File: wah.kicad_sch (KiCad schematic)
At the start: 32 parts, among them J3 Barrel_Jack_Switch, J4 In, J5 Out, SW2 SW_Push_3PDT, U1 L78L05_TO92, U2 TL072

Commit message: improve pcb
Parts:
- C1, C10, C11, C12, C3, C4, C5, C6, C7, C8, C9: footprint Capacitor_THT:C_Rect_L4.6mm_W2.0mm_P2.50mm_MKS02_FKP02 -> Capacitor_THT:C_Rect_L7.0mm_W2.5mm_P5.00mm
- C2: footprint Capacitor_THT:CP_Radial_D5.0mm_P2.50mm -> Capacitor_THT:C_Rect_L7.0mm_W2.5mm_P5.00mm
- R1, R2, R3, R4, R5, R6, R7, R8, R9: footprint Resistor_THT:R_Axial_DIN0207_L6.3mm_D2.5mm_P10.16mm_Horizontal -> Resistor_THT:R_Axial_DIN0207_L6.3mm_D2.5mm_P7.62mm_Horizontal
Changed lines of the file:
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@@
 		(title "Wah")
 		(date "2025-10-29")
-		(rev "0.1")
+		(rev "0.2")
 		(company "KnightHill Engineering")
 	)
@@
 			)
 		)
-		(property "Footprint" "Resistor_THT:R_Axial_DIN0207_L6.3mm_D2.5mm_P10.16mm_Horizontal"
+		(property "Footprint" "Resistor_THT:R_Axial_DIN0207_L6.3mm_D2.5mm_P7.62mm_Horizontal"
 			(at 297.18 152.908 90)
 			(effects
@@
 			)
 		)
-		(property "Footprint" "Resistor_THT:R_Axial_DIN0207_L6.3mm_D2.5mm_P10.16mm_Horizontal"
+		(property "Footprint" "Resistor_THT:R_Axial_DIN0207_L6.3mm_D2.5mm_P7.62mm_Horizontal"
 			(at 234.95 66.548 90)
 			(effects
@@
 			)
 		)
-		(property "Footprint" "Capacitor_THT:C_Rect_L4.6mm_W2.0mm_P2.50mm_MKS02_FKP02"
+		(property "Footprint" "Capacitor_THT:C_Rect_L7.0mm_W2.5mm_P5.00mm"
 			(at 168.6052 237.49 0)
 			(effects
@@
 			)
 		)
-		(property "Footprint" "Resistor_THT:R_Axial_DIN0207_L6.3mm_D2.5mm_P10.16mm_Horizontal"
+		(property "Footprint" "Resistor_THT:R_Axial_DIN0207_L6.3mm_D2.5mm_P7.62mm_Horizontal"
 			(at 78.74 65.278 90)
 			(effects
@@
 			)
 		)
-		(property "Footprint" "Resistor_THT:R_Axial_DIN0207_L6.3mm_D2.5mm_P10.16mm_Horizontal"
+		(property "Footprint" "Resistor_THT:R_Axial_DIN0207_L6.3mm_D2.5mm_P7.62mm_Horizontal"
 			(at 137.16 67.818 90)
 			(effects
@@
 			)
 		)
-		(property "Footprint" "Capacitor_THT:C_Rect_L4.6mm_W2.0mm_P2.50mm_MKS02_FKP02"
+		(property "Footprint" "Capacitor_THT:C_Rect_L7.0mm_W2.5mm_P5.00mm"
 			(at 155.9052 237.49 0)
 			(effects
@@
 			)
 		)
-		(property "Footprint" "Capacitor_THT:C_Rect_L4.6mm_W2.0mm_P2.50mm_MKS02_FKP02"
+		(property "Footprint" "Capacitor_THT:C_Rect_L7.0mm_W2.5mm_P5.00mm"
 			(at 195.2752 237.49 0)
 			(effects
@@
 			)
 		)
-		(property "Footprint" "Capacitor_THT:C_Rect_L4.6mm_W2.0mm_P2.50mm_MKS02_FKP02"
+		(property "Footprint" "Capacitor_THT:C_Rect_L7.0mm_W2.5mm_P5.00mm"
 			(at 249.8852 74.93 0)
 			(effects
@@
 			)
 		)
-		(property "Footprint" "Capacitor_THT:C_Rect_L4.6mm_W2.0mm_P2.50mm_MKS02_FKP02"
+		(property "Footprint" "Capacitor_THT:C_Rect_L7.0mm_W2.5mm_P5.00mm"
 			(at 88.5952 74.93 0)
 			(effects
@@
 			)
 		)
-		(property "Footprint" "Capacitor_THT:C_Rect_L4.6mm_W2.0mm_P2.50mm_MKS02_FKP02"
+		(property "Footprint" "Capacitor_THT:C_Rect_L7.0mm_W2.5mm_P5.00mm"
 			(at 152.4 65.0748 0)
 			(effects
@@
 			)
 		)
-		(property "Footprint" "Capacitor_THT:C_Rect_L4.6mm_W2.0mm_P2.50mm_MKS02_FKP02"
+		(property "Footprint" "Capacitor_THT:C_Rect_L7.0mm_W2.5mm_P5.00mm"
 			(at 247.3452 237.49 0)
 			(effects
@@
 			)
 		)
-		(property "Footprint" "Capacitor_THT:C_Rect_L4.6mm_W2.0mm_P2.50mm_MKS02_FKP02"
+		(property "Footprint" "Capacitor_THT:C_Rect_L7.0mm_W2.5mm_P5.00mm"
 			(at 101.6 62.5348 0)
 			(effects
@@
 			)
 		)
-		(property "Footprint" "Capacitor_THT:CP_Radial_D5.0mm_P2.50mm"
+		(property "Footprint" "Capacitor_THT:C_Rect_L7.0mm_W2.5mm_P5.00mm"
 			(at 143.2052 237.49 0)
 			(effects
@@
 			)
 		)
-		(property "Footprint" "Resistor_THT:R_Axial_DIN0207_L6.3mm_D2.5mm_P10.16mm_Horizontal"
+		(property "Footprint" "Resistor_THT:R_Axial_DIN0207_L6.3mm_D2.5mm_P7.62mm_Horizontal"
 			(at 106.172 52.07 90)
 			(effects
@@
 			)
 		)
-		(property "Footprint" "Resistor_THT:R_Axial_DIN0207_L6.3mm_D2.5mm_P10.16mm_Horizontal"
+		(property "Footprint" "Resistor_THT:R_Axial_DIN0207_L6.3mm_D2.5mm_P7.62mm_Horizontal"
 			(at 243.332 57.15 90)
 			(effects
@@
 			)
 		)
-		(property "Footprint" "Capacitor_THT:C_Rect_L4.6mm_W2.0mm_P2.50mm_MKS02_FKP02"
+		(property "Footprint" "Capacitor_THT:C_Rect_L7.0mm_W2.5mm_P5.00mm"
 			(at 216.8652 74.93 0)
 			(effects
@@
 			)
 		)
-		(property "Footprint" "Resistor_THT:R_Axial_DIN0207_L6.3mm_D2.5mm_P10.16mm_Horizontal"
+		(property "Footprint" "Resistor_THT:R_Axial_DIN0207_L6.3mm_D2.5mm_P7.62mm_Horizontal"
 			(at 223.52 229.108 90)
 			(effects
@@
 			)
 		)
-		(property "Footprint" "Capacitor_THT:C_Rect_L4.6mm_W2.0mm_P2.50mm_MKS02_FKP02"
+		(property "Footprint" "Capacitor_THT:C_Rect_L7.0mm_W2.5mm_P5.00mm"
 			(at 215.5952 237.49 0)
 			(effects
@@
 			)
 		)
-		(property "Footprint" "Resistor_THT:R_Axial_DIN0207_L6.3mm_D2.5mm_P10.16mm_Horizontal"
+		(property "Footprint" "Resistor_THT:R_Axial_DIN0207_L6.3mm_D2.5mm_P7.62mm_Horizontal"
 			(at 155.702 72.39 90)
 			(effects
@@
 			)
 		)
-		(property "Footprint" "Resistor_THT:R_Axial_DIN0207_L6.3mm_D2.5mm_P10.16mm_Horizontal"
+		(property "Footprint" "Resistor_THT:R_Axial_DIN0207_L6.3mm_D2.5mm_P7.62mm_Horizontal"
 			(at 234.188 233.68 90)
 			(effects
@@
 			)
 		)
-		(property "Footprint" "Capacitor_THT:C_Rect_L4.6mm_W2.0mm_P2.50mm_MKS02_FKP02"
+		(property "Footprint" "Capacitor_THT:C_Rect_L7.0mm_W2.5mm_P5.00mm"
 			(at 228.6 63.8048 0)
 			(effects

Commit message: improve pcb
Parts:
- added GND1, GND2: ~, TestPoint:TestPoint_THTPad_1.5x1.5mm_Drill0.7mm, symbol Connector:TestPoint
- added TP_IN1, TP_OUT1: TestPoint, TestPoint:TestPoint_THTPad_1.5x1.5mm_Drill0.7mm, symbol Connector:TestPoint
- renumbered C10 to C1, C9 to C10, C7 to C11, C8 to C12, C11 to C2, C2 to C3, C3 to C4, C4 to C5, C12 to C6, C1 to C7, C5 to C8, C6 to C9, J3 to J1, J4 to J2, J5 to J3, R6 to R1, R7 to R2, R8 to R3, R9 to R4, R4 to R5, R5 to R6, R2 to R7, R3 to R8, R1 to R9, SW2 to SW1, U2 to U1, U1 to U2
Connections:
- net FX_IN: now also TP_IN1.1
- net FX_OUT: now also TP_OUT1.1
- net GND: now also GND1.1, GND2.1
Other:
- moved on the sheet: C1, C11, C12, C2, C6, C9, R1, R2, R3, R4, R7, R8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

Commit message: fix errors
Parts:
- removed C10: 100u, Capacitor_THT:C_Rect_L7.0mm_W2.5mm_P5.00mm, symbol Device:C
- added C13: 100u, Capacitor_THT:CP_Radial_D6.3mm_P2.50mm, symbol Device:C_Polarized
- added TP_5V1, TP_VREF1: TestPoint, TestPoint:TestPoint_THTPad_1.5x1.5mm_Drill0.7mm, symbol Connector:TestPoint
- C3: footprint Capacitor_THT:C_Rect_L7.0mm_W2.5mm_P5.00mm -> Capacitor_THT:CP_Radial_D6.3mm_P2.50mm
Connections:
- net AUDIO_IN: now also C6.2, R4.1; no longer U1.1, U1.2 (-)
- net AUDIO_OUT: now also C11.1, C9.1; no longer R1.1
- net FX_IN: now also R1.1; no longer C11.1, C9.1
- net FX_OUT: now also U1.1, U1.2 (-); no longer C6.2, R4.1
- net GND: now also C13.2
- net VREF: now also C13.1, TP_VREF1.1
- net at C7.1, C8.1, R5.1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: now also TP_5V1.1
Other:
- moved on the sheet: TP_IN1, TP_OUT1

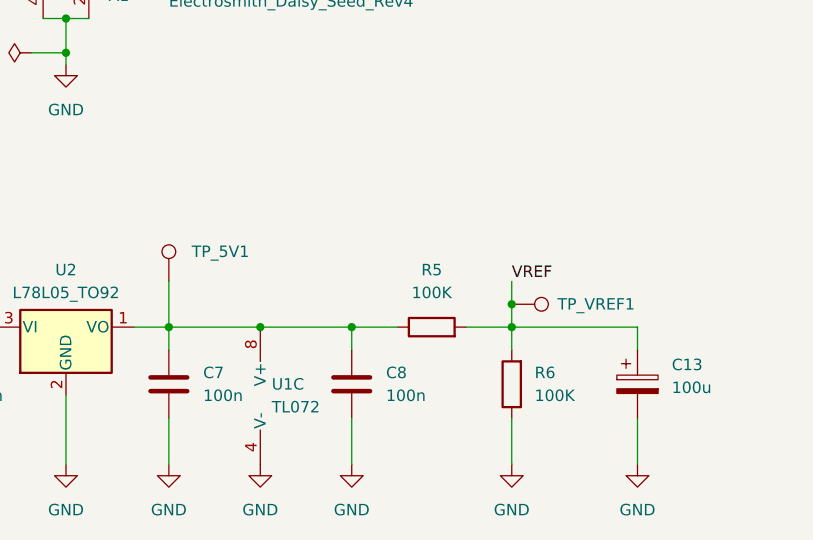
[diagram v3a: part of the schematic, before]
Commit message: remove probes
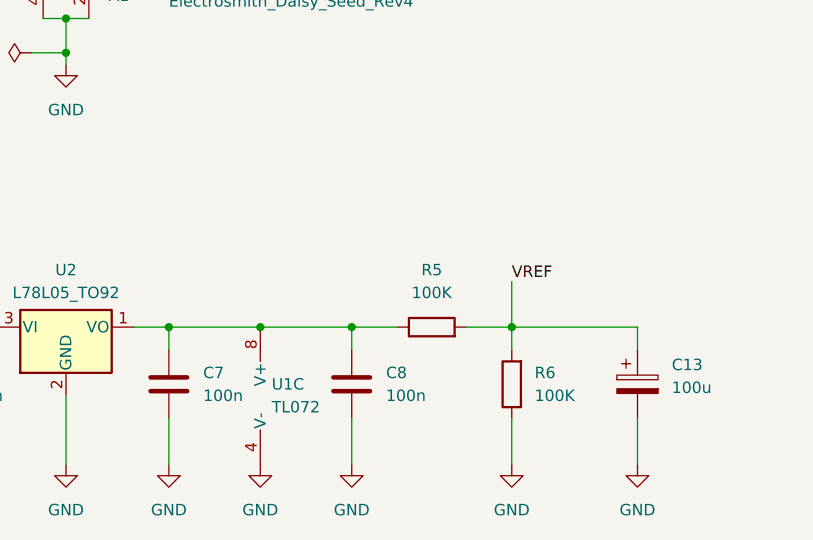
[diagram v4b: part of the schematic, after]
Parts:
- removed TP_5V1, TP_VREF1: TestPoint, TestPoint:TestPoint_THTPad_1.5x1.5mm_Drill0.7mm, symbol Connector:TestPoint
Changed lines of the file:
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@@
 	)
 	(junction
-		(at 232.41 224.79)
-		(diameter 0)
-		(color 0 0 0 0)
-	)
-	(junction
 		(at 240.03 64.77)
 		(diameter 0)
@@
 	(wire
 		(pts
-			(xy 232.41 224.79) (xy 232.41 227.33)
+			(xy 232.41 222.25) (xy 232.41 227.33)
 		)
 		(stroke
@@
 	(wire
 		(pts
-			(xy 194.31 222.25) (xy 194.31 227.33)
-		)
-		(stroke
-			(width 0)
-			(type default)
-		)
-	)
-	(wire
-		(pts
 			(xy 167.64 242.57) (xy 167.64 237.49)
 		)
@@
 	(wire
 		(pts
-			(xy 232.41 222.25) (xy 232.41 224.79)
-		)
-		(stroke
-			(width 0)
-			(type default)
-		)
-	)
-	(wire
-		(pts
 			(xy 142.24 242.57) (xy 142.24 237.49)
 		)
@@
 	)
 	(symbol
-		(lib_id "Connector:TestPoint")
-		(at 194.31 222.25 0)
-		(unit 1)
-		(exclude_from_sim no)
-		(in_bom yes)
-		(on_board yes)
-		(dnp no)
-		(fields_autoplaced yes)
-		(property "Reference" "TP_5V1"
-			(at 196.85 218.9479 0)
-			(effects
-				(font
-					(size 1.27 1.27)
-				)
-				(justify left)
-			)
-		)
-		(property "Value" "TestPoint"
-			(at 196.85 220.2179 0)
-			(effects
-				(font
-					(size 1.27 1.27)
-				)
-				(justify left)
-				(hide yes)
-			)
-		)
-		(property "Footprint" "TestPoint:TestPoint_THTPad_1.5x1.5mm_Drill0.7mm"
-			(at 199.39 222.25 0)
-			(effects
-				(font
-					(size 1.27 1.27)
-				)
-				(hide yes)
-			)
-		)
-		(property "Datasheet" "~"
-			(at 199.39 222.25 0)
-			(effects
-				(font
-					(size 1.27 1.27)
-				)
-				(hide yes)
-			)
-		)
-		(property "Description" "test point"
-			(at 194.31 222.25 0)
-			(effects
-				(font
-					(size 1.27 1.27)
-				)
-				(hide yes)
-			)
-		)
-		(pin "1"
-		)
-		(instances
-			(project "wah"
-				(path "/93d00cbf-8e4b-443f-bc57-0c283a060166"
-					(reference "TP_5V1")
-					(unit 1)
-				)
-			)
-		)
-	)
-	(symbol
 		(lib_id "CustomSymbols:SW_Push_3PDT")
 		(at 285.75 138.43 0)
@@
 					(unit 1)
 				)
-			)
-		)
-	)
-	(symbol
-		(lib_id "Connector:TestPoint")
-		(at 232.41 224.79 270)
-		(unit 1)
-		(exclude_from_sim no)
-		(in_bom yes)
-		(on_board yes)
-		(dnp no)
-		(fields_autoplaced yes)
-		(property "Reference" "TP_VREF1"
-			(at 237.49 224.7899 90)
-			(effects
-				(font
-					(size 1.27 1.27)
-				)
-				(justify left)
-			)
-		)
-		(property "Value" "TestPoint"
-			(at 234.4421 227.33 0)
-			(effects
-				(font
-					(size 1.27 1.27)
-				)
-				(justify left)
-				(hide yes)
-			)
-		)
-		(property "Footprint" "TestPoint:TestPoint_THTPad_1.5x1.5mm_Drill0.7mm"
-			(at 232.41 229.87 0)
-			(effects
-				(font
-					(size 1.27 1.27)
-				)
-				(hide yes)
-			)
-		)
-		(property "Datasheet" "~"
-			(at 232.41 229.87 0)
-			(effects
-				(font
-					(size 1.27 1.27)
-				)
-				(hide yes)
-			)
-		)
-		(property "Description" "test point"
-			(at 232.41 224.79 0)
-			(effects
-				(font
-					(size 1.27 1.27)
-				)
-				(hide yes)
-			)
-		)
-		(pin "1"
-		)
-		(instances
-			(project "wah"
-				(path "/93d00cbf-8e4b-443f-bc57-0c283a060166"
-					(reference "TP_VREF1")
-					(unit 1)
-				)
